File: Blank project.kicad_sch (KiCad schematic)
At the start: 0 parts

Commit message: added resistor and cap.
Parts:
- added C1: C_Polarized_US, symbol Device:C_Polarized_US
- added R1: R_US, symbol Device:R_US
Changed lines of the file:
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@@
 (kicad_sch (version 20220929) (generator eeschema)
   (paper "A4")
+  (symbol (lib_id "Device:R_US") (at 111.76 90.17 0) (unit 1)
+    (in_bom yes) (on_board yes) (dnp no) (fields_autoplaced)
+    (default_instance (reference "R1") (unit 1) (value "R_US") (footprint ""))
+    (property "Reference" "R1" (at 114.3 89.535 0)
+      (effects (font (size 1.27 1.27)) (justify left))
+    )
+    (property "Value" "R_US" (at 114.3 92.075 0)
+      (effects (font (size 1.27 1.27)) (justify left))
+    )
+    (property "Footprint" "" (at 112.776 90.424 90)
+      (effects (font (size 1.27 1.27)) hide)
+    )
+    (property "Datasheet" "~" (at 111.76 90.17 0)
+      (effects (font (size 1.27 1.27)) hide)
+    )
+    (pin "1")
+    (pin "2")
+  )
+  (symbol (lib_id "Device:C_Polarized_US") (at 129.54 91.44 0) (unit 1)
+    (in_bom yes) (on_board yes) (dnp no) (fields_autoplaced)
+    (default_instance (reference "C1") (unit 1) (value "C_Polarized_US") (footprint ""))
+    (property "Reference" "C1" (at 133.35 90.17 0)
+      (effects (font (size 1.27 1.27)) (justify left))
+    )
+    (property "Value" "C_Polarized_US" (at 133.35 92.71 0)
+      (effects (font (size 1.27 1.27)) (justify left))
+    )
+    (property "Footprint" "" (at 129.54 91.44 0)
+      (effects (font (size 1.27 1.27)) hide)
+    )
+    (property "Datasheet" "~" (at 129.54 91.44 0)
+      (effects (font (size 1.27 1.27)) hide)
+    )
+    (pin "1")
+    (pin "2")
+  )
   (sheet_instances
     (path "/" (page "1"))
   )
+  (symbol_instances
+    (path "/ccdc9c70-b584-4a32-8e24-1afd9eb614b4"
+      (reference "C1") (unit 1) (value "C_Polarized_US") (footprint "")
+    )
+    (path "/208ec824-a215-4c9c-b4c3-1cbb604593a7"
+      (reference "R1") (unit 1) (value "R_US") (footprint "")
+    )
+  )
 )

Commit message: added capacitor in experimental branch.
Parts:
- added C1: C_Polarized_US, symbol Device:C_Polarized_US
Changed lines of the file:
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@@
+    (pin "2")
+  )
+  (symbol (lib_id "Device:C_Polarized_US") (at 158.75 91.44 0) (unit 1)
+    (in_bom yes) (on_board yes) (dnp no) (fields_autoplaced)
+    (default_instance (reference "C1") (unit 1) (value "C_Polarized_US") (footprint ""))
+    (property "Reference" "C1" (at 162.56 90.17 0)
+      (effects (font (size 1.27 1.27)) (justify left))
+    )
+    (property "Value" "C_Polarized_US" (at 162.56 92.71 0)
+      (effects (font (size 1.27 1.27)) (justify left))
+    )
+    (property "Footprint" "" (at 158.75 91.44 0)
+      (effects (font (size 1.27 1.27)) hide)
+    )
+    (property "Datasheet" "~" (at 158.75 91.44 0)
+      (effects (font (size 1.27 1.27)) hide)
+    )
+    (pin "1")
     (pin "2")
   )
@@
       (reference "C1") (unit 1) (value "C_Polarized_US") (footprint "")
     )
+    (path "/908198ca-6145-4356-8137-d8d535e5be4c"
+      (reference "C2") (unit 1) (value "C_Polarized_US") (footprint "")
+    )
     (path "/208ec824-a215-4c9c-b4c3-1cbb604593a7"

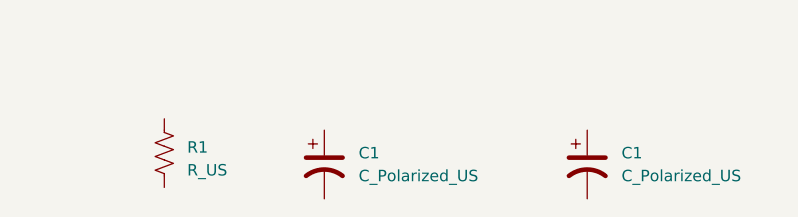
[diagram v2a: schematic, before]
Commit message: added text project name.
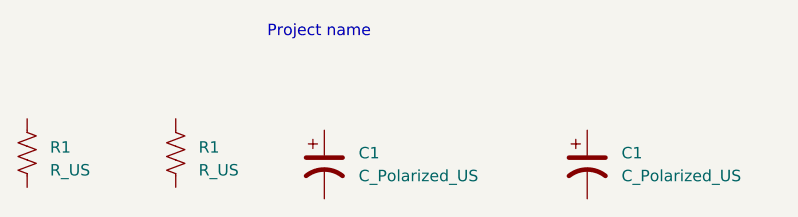
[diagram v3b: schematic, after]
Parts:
- added R1: R_US, symbol Device:R_US
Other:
- note added: "Project name"
- moved on the sheet: R1
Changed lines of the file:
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@@
 (kicad_sch (version 20220929) (generator eeschema)
   (paper "A4")
-  (symbol (lib_id "Device:R_US") (at 111.76 90.17 0) (unit 1)
+  (text "Project name" (at 123.19 77.47 0)
+    (effects (font (size 1.27 1.27)) (justify left bottom))
+  )
+  (symbol (lib_id "Device:R_US") (at 113.03 90.17 0) (unit 1)
     (in_bom yes) (on_board yes) (dnp no) (fields_autoplaced)
     (default_instance (reference "R1") (unit 1) (value "R_US") (footprint ""))
-    (property "Reference" "R1" (at 114.3 89.535 0)
+    (property "Reference" "R1" (at 115.57 89.535 0)
       (effects (font (size 1.27 1.27)) (justify left))
     )
-    (property "Value" "R_US" (at 114.3 92.075 0)
+    (property "Value" "R_US" (at 115.57 92.075 0)
       (effects (font (size 1.27 1.27)) (justify left))
     )
-    (property "Footprint" "" (at 112.776 90.424 90)
+    (property "Footprint" "" (at 114.046 90.424 90)
       (effects (font (size 1.27 1.27)) hide)
     )
-    (property "Datasheet" "~" (at 111.76 90.17 0)
+    (property "Datasheet" "~" (at 113.03 90.17 0)
       (effects (font (size 1.27 1.27)) hide)
     )
@@
     (pin "2")
   )
+  (symbol (lib_id "Device:R_US") (at 96.52 90.17 0) (unit 1)
+    (in_bom yes) (on_board yes) (dnp no) (fields_autoplaced)
+    (default_instance (reference "R1") (unit 1) (value "R_US") (footprint ""))
+    (property "Reference" "R1" (at 99.06 89.535 0)
+      (effects (font (size 1.27 1.27)) (justify left))
+    )
+    (property "Value" "R_US" (at 99.06 92.075 0)
+      (effects (font (size 1.27 1.27)) (justify left))
+    )
+    (property "Footprint" "" (at 97.536 90.424 90)
+      (effects (font (size 1.27 1.27)) hide)
+    )
+    (property "Datasheet" "~" (at 96.52 90.17 0)
+      (effects (font (size 1.27 1.27)) hide)
+    )
+    (pin "1")
+    (pin "2")
+  )
   (sheet_instances
     (path "/" (page "1"))
@@
       (reference "R1") (unit 1) (value "R_US") (footprint "")
     )
+    (path "/d6dc20b6-4d7d-492c-838d-aaad3a005e0c"
+      (reference "R2") (unit 1) (value "R_US") (footprint "")
+    )
   )

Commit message: Update Blank project.kicad_sch
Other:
- note added: "example change on github (was Project name)"
- note removed: "Project name"
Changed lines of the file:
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@@
 (kicad_sch (version 20220929) (generator eeschema)
   (paper "A4")
-  (text "Project name" (at 123.19 77.47 0)
+  (text "example change on github (was Project name)" (at 123.19 77.47 0)
     (effects (font (size 1.27 1.27)) (justify left bottom))
   )
